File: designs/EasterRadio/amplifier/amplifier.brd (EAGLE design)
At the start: 33 x 36 mm, 14 parts, among them IC1 PAM8403DR, J1 STX-3120-3BM, J2 S2B-NSHSS-TB, J3 S2B-NSHSS-TB

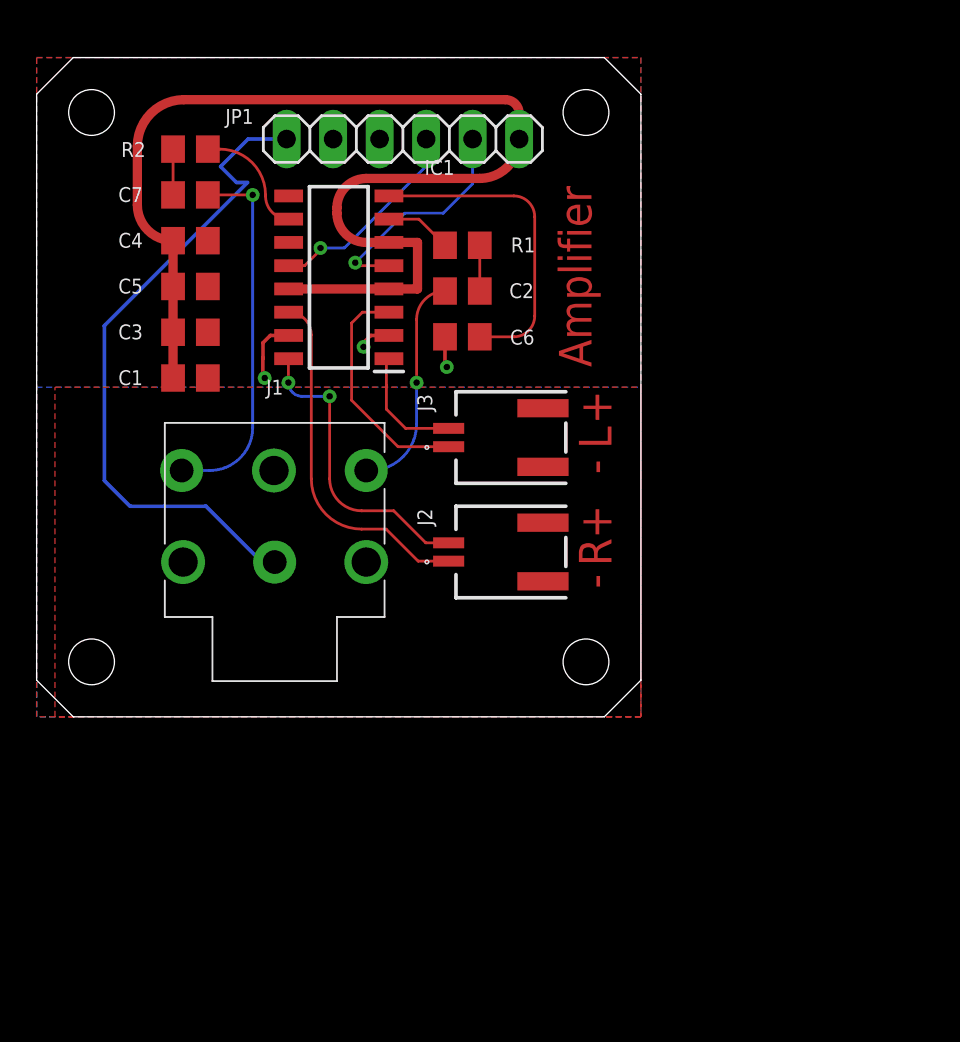
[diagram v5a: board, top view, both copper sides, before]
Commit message: added esd for rs232 to can
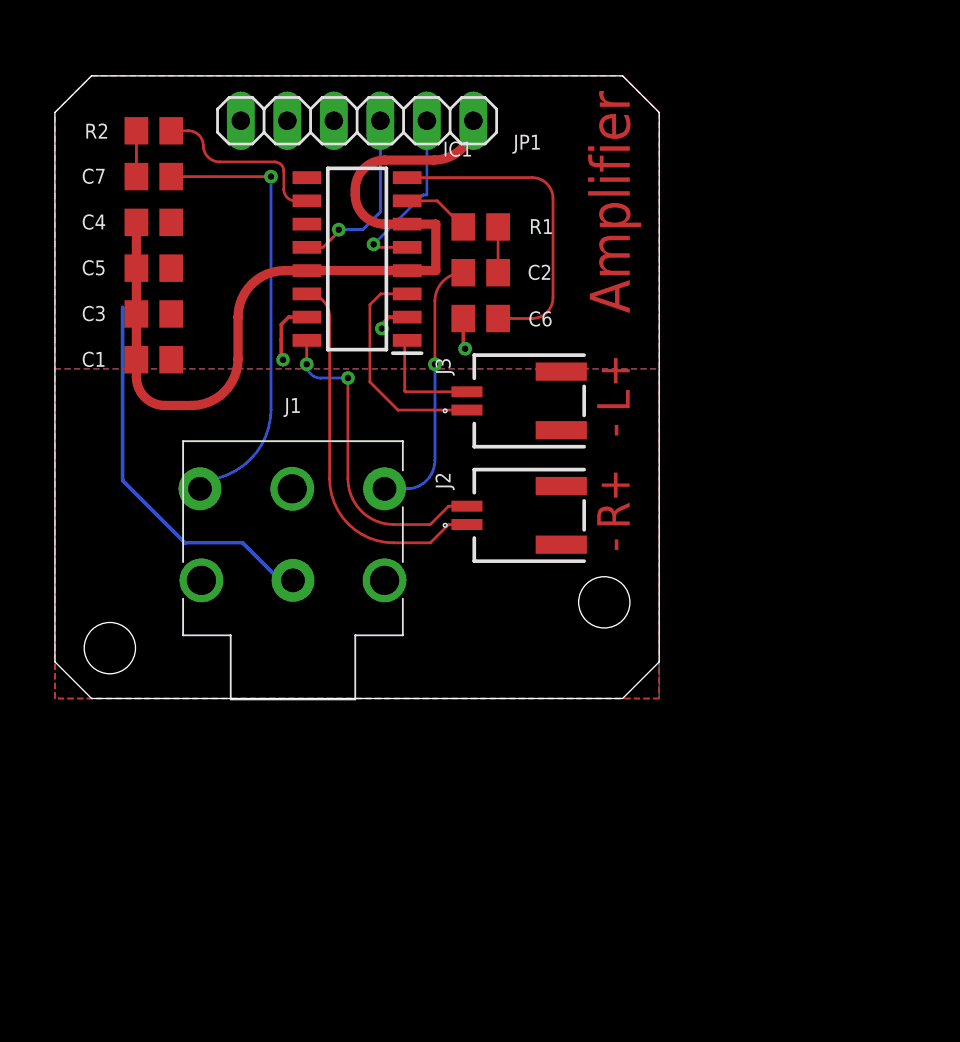
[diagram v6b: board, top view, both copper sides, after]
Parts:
- moved JP1 2.69 mm to (16.5, 31.6)
- moved C1 2.24 mm to (5.40, 18.5)
- moved C3 2.24 mm to (5.40, 21.0)
- moved C4 2.24 mm to (5.40, 26.0)
- moved C5 2.24 mm to (5.40, 23.5)
- moved C7 2.24 mm to (5.40, 28.5)
- moved J2 2.24 mm to (22.5, 10.5)
- moved J3 2.24 mm to (22.5, 16.8)
- moved R2 2.24 mm to (5.40, 31.0)
- moved C2 1.41 mm to (23.2, 23.2)
- moved C6 1.41 mm to (23.2, 20.8)
- moved IC1 1.41 mm to (16.5, 24.0)
- moved J1 1.41 mm to (13.0, 7.00)
- moved R1 1.41 mm to (23.2, 25.8)
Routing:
- net 3.3V: track 63.5 -> 45.7 mm
- net AGND: track 43.7 -> 28.0 mm
- net INR: track 20.0 -> 24.1 mm
- net IC2_INR: track 6.03 -> 9.58 mm
- net INL: track 11.7 -> 14.3 mm
- net !MUTE: track 12.5 -> 9.98 mm
- net !SHDN: track 11.3 -> 9.85 mm
- net OUT_R+: track 16.3 -> 17.3 mm
- net OUT_R-: track 19.0 -> 20.0 mm
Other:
- board size 33 x 36 mm -> 33 x 34 mm

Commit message: added mainboard layout and new 3.5mm jack
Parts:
- removed J1: STX-3120-3BM, MouserUseful:STX31203BM
- added J4: SJ-3523-SMT-TR, MouserUseful:SJ3523SMTTR
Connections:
- removed net N$17: JP1.3
- removed net N$18: JP1.2
- net AGND: now also J4.1; no longer J1.1
- net INL: now also J4.2, JP1.3; no longer J1.2
- net INR: now also J4.3, JP1.2; no longer J1.5
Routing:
- net INL: track 14.3 -> 41.2 mm, vias 1 -> 2
- net INR: track 24.1 -> 31.3 mm, vias 1 -> 2
- net AGND: track 28.0 -> 22.3 mm
- net OUT_L-: track 12.4 -> 11.9 mm
- net OUT_R+: track 17.3 -> 17.8 mm
